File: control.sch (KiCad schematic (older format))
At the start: 47 parts, among them J401 CHG, J402 CTRL, J403 SOICbite, J404 RS485, SW401 RESET, SW402 USER, U401 STM32F072CBTx, U402 CH340G, U403 SP3485EN, Y401 12MHz

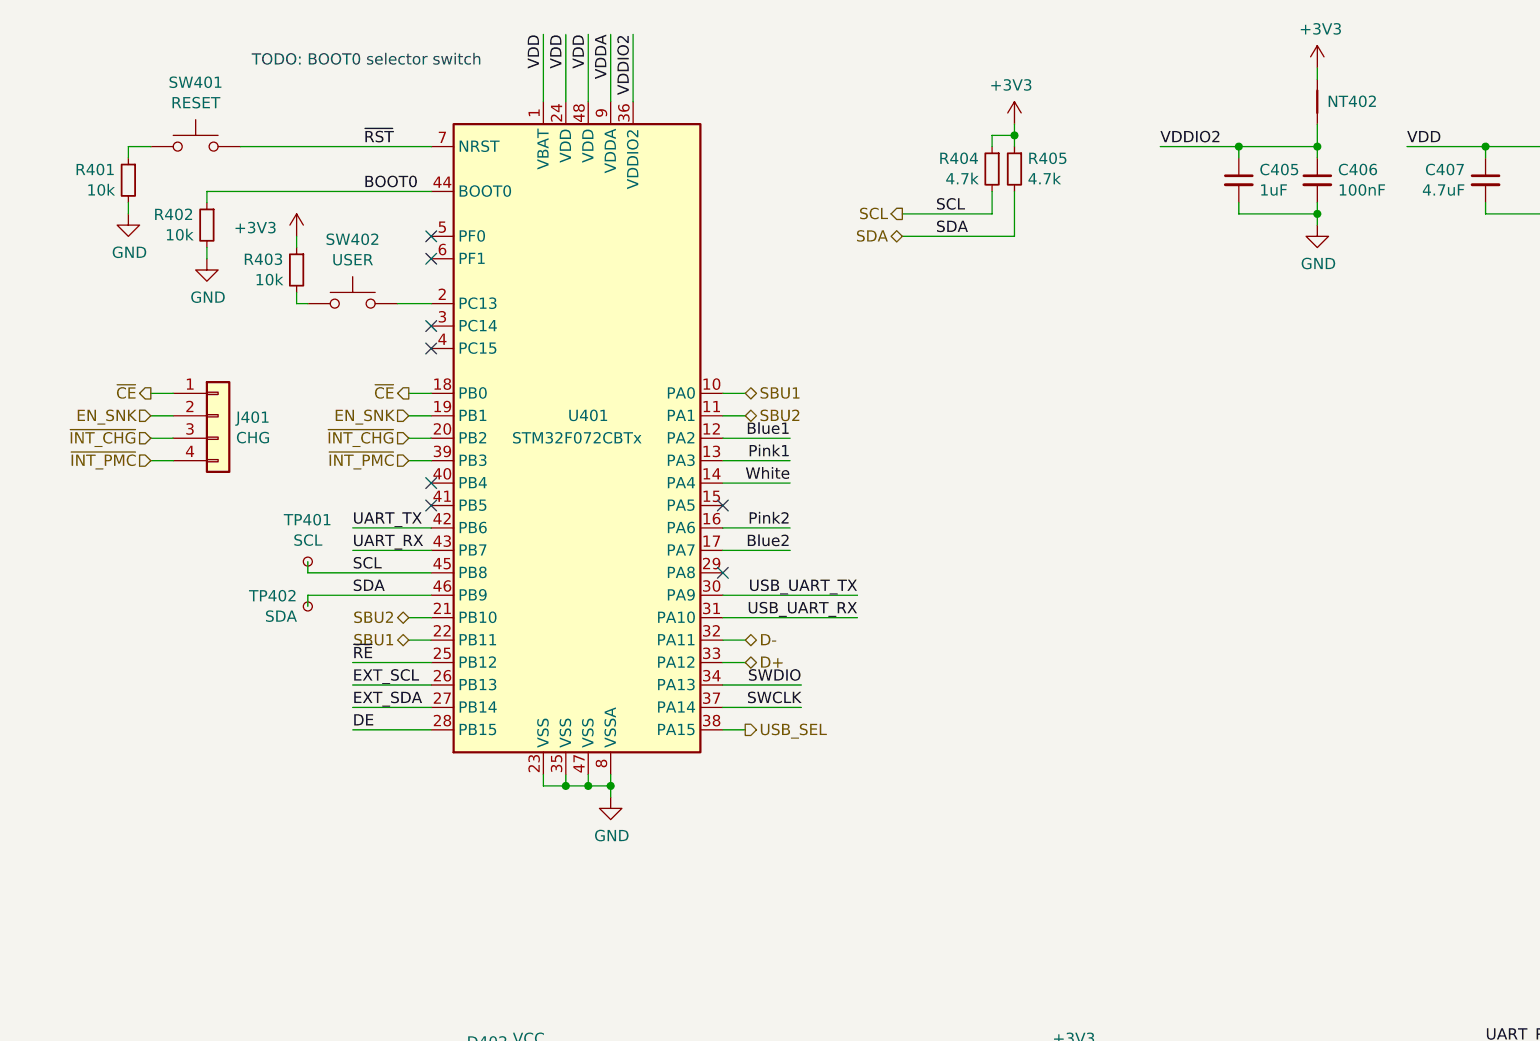
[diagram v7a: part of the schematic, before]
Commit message: added a crystal
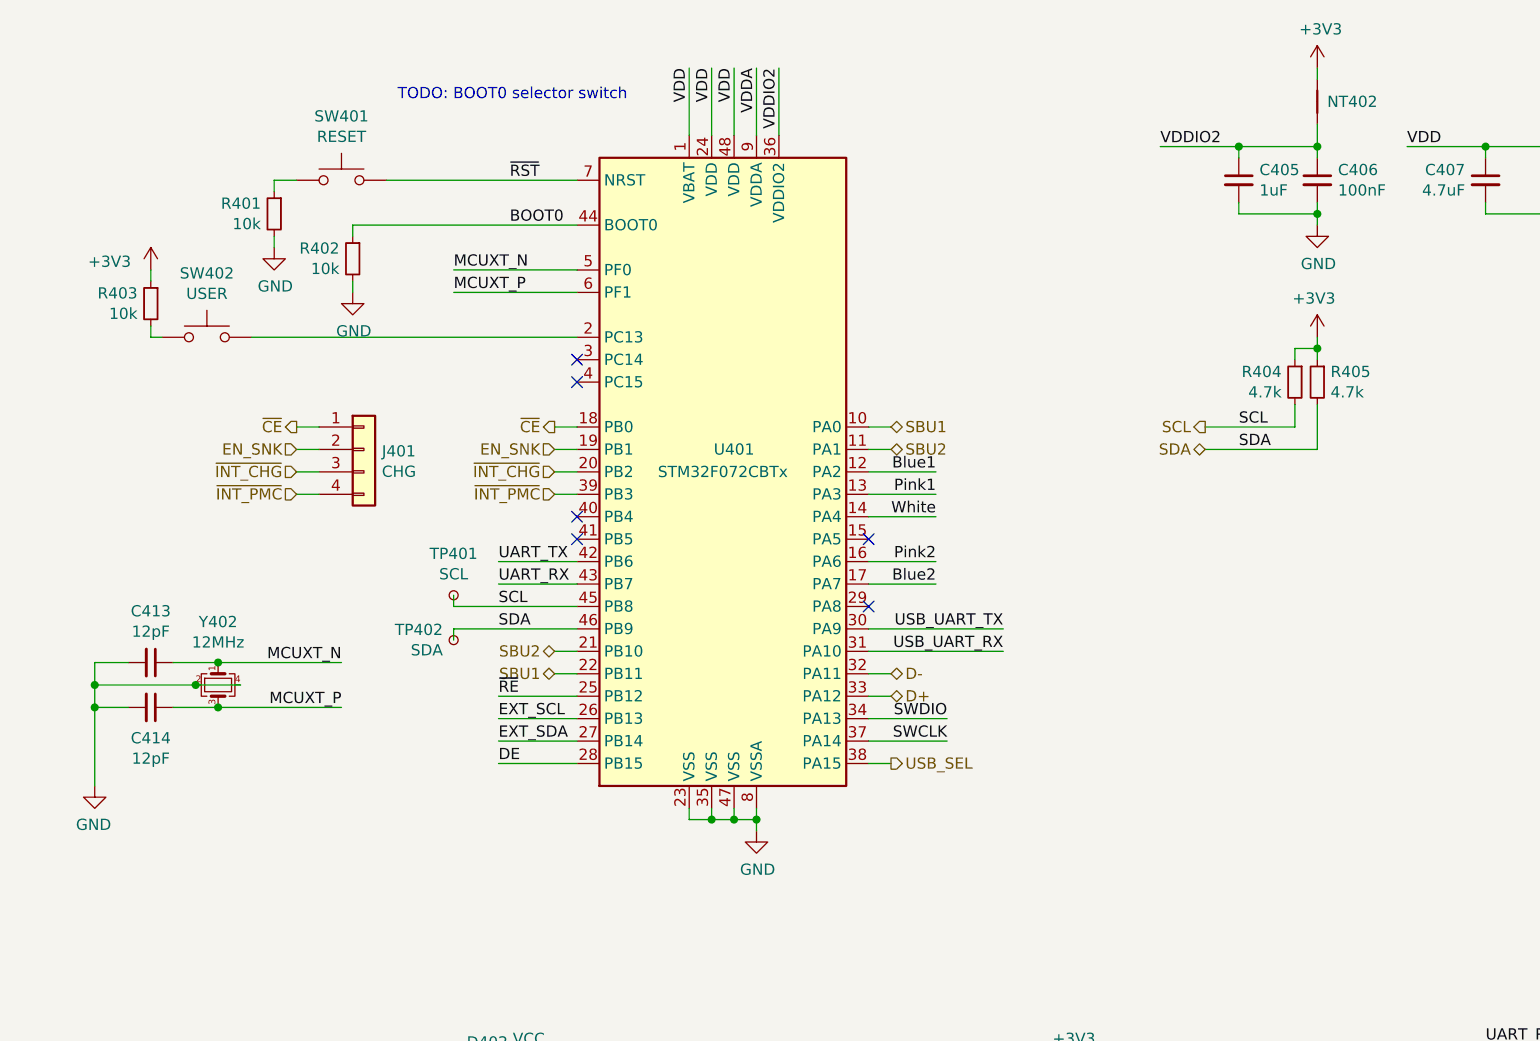
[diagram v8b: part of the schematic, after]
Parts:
- added C413, C414: 12pF, Capacitor_SMD:C_0402_1005Metric, symbol Device:C_Small
- added Y402: 12MHz, Crystal:Crystal_SMD_3225-4Pin_3.2x2.5mm, symbol Device:Crystal_GND24_Small
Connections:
- net GND: now also C413.2, C414.2, Y402.2, Y402.4
- net MCUXT_N: now reaches U401.5 (PF0)
- net MCUXT_N: now also C413.1, Y402.1
- net MCUXT_P: now reaches U401.6 (PF1)
- net MCUXT_P: now also C414.1, Y402.3
- no-connect marks 22 -> 20
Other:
- moved on the sheet: J401, R401, R402, R403, R404, R405, SW401, SW402, TP401, TP402, U401
